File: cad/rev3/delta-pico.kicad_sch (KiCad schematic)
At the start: 70 parts, among them J1 Conn_01x02, J2 Conn_01x14, J3 Conn_01x08, J4 Conn_01x04, J5 Conn_01x03, SW1 SW_SPDT, SW10 SW_Push, SW11 SW_Push, SW12 SW_Push, SW13 SW_Push, SW14 SW_Push, SW15 SW_Push, SW16 SW_Push, SW17 SW_Push, SW18 SW_Push, SW19 SW_Push, SW2 SW_Push, SW20 SW_Push, SW21 SW_Push, SW22 SW_Push, SW23 SW_Push, SW24 SW_Push, SW25 SW_Push, SW26 SW_Push, SW27 SW_Push, SW28 SW_Push, SW29 SW_Push, SW3 SW_Push, SW30 SW_Push, SW31 SW_Push, SW4 SW_Push, SW5 SW_Push, SW6 SW_Push, SW7 SW_Push, SW8 SW_Push, SW9 SW_Push, U1 PCF8574A, U2 PCF8574A, U3 Pico, U4 24LC16

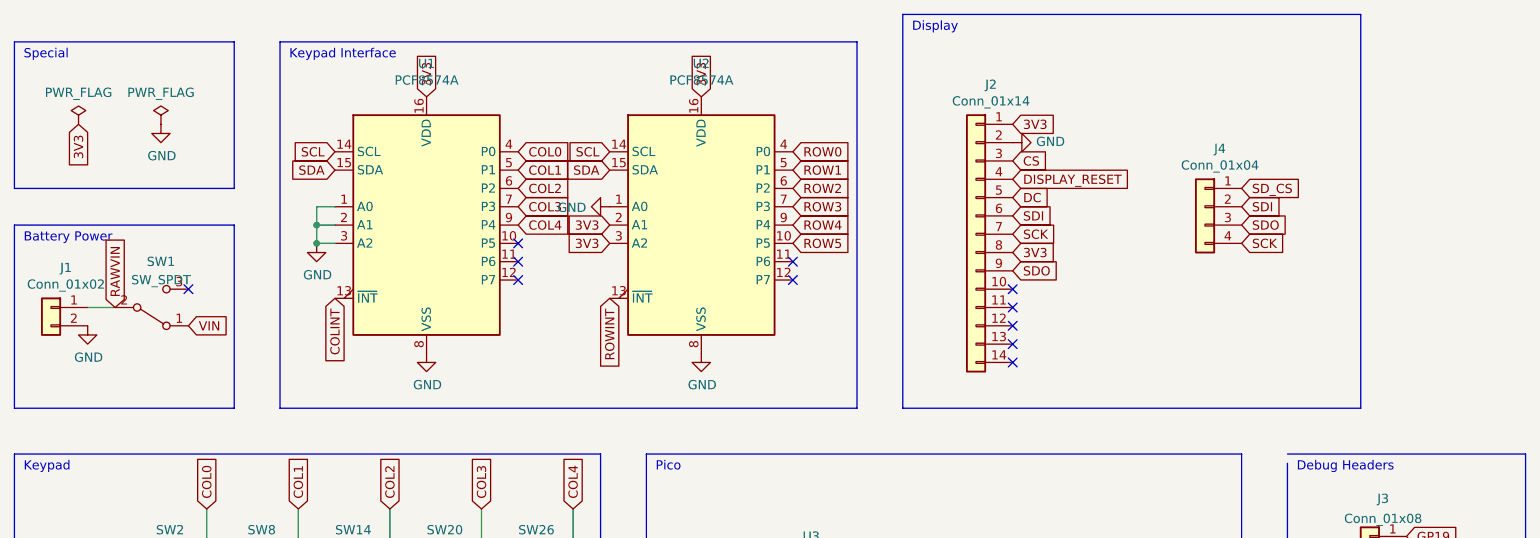
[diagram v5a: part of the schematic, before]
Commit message: Add Schottky diode on VSYS
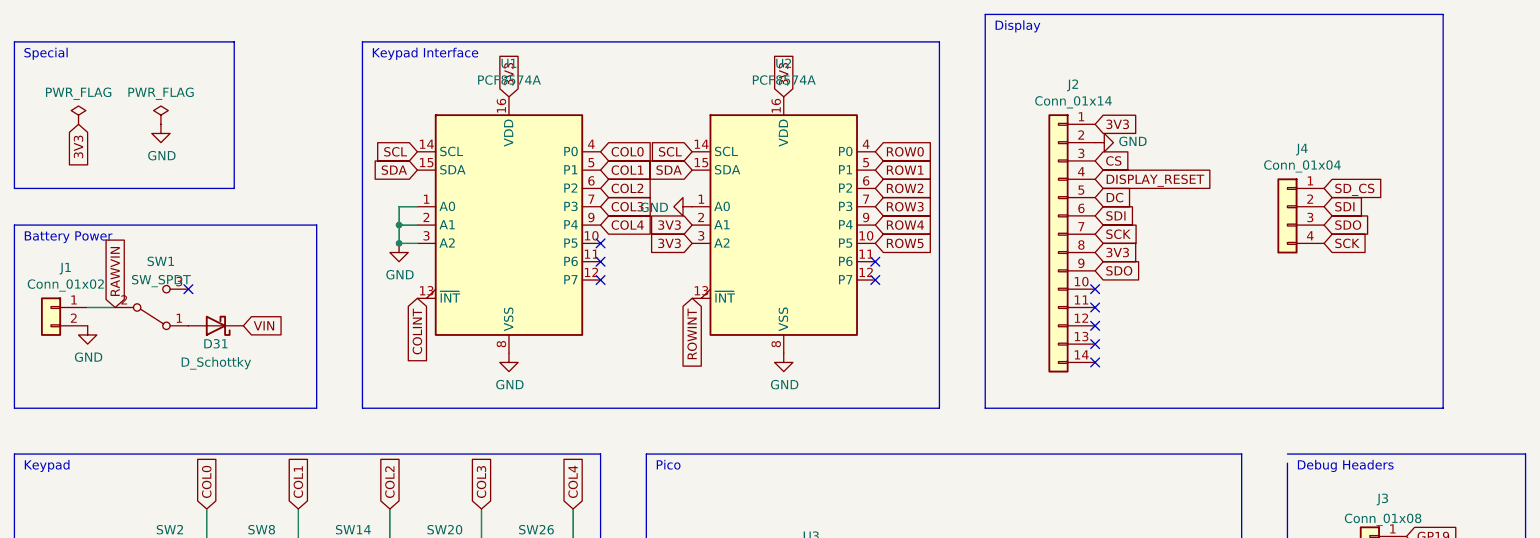
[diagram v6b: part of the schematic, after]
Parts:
- added D31: D_Schottky, Diode_SMD:D_SOD-123, symbol Device:D_Schottky
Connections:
- net VIN: now also D31.1 (K); no longer SW1.1 (A)
- new net: D31.2 (A), SW1.1 (A)
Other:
- moved on the sheet: J2, J4, U1, U2

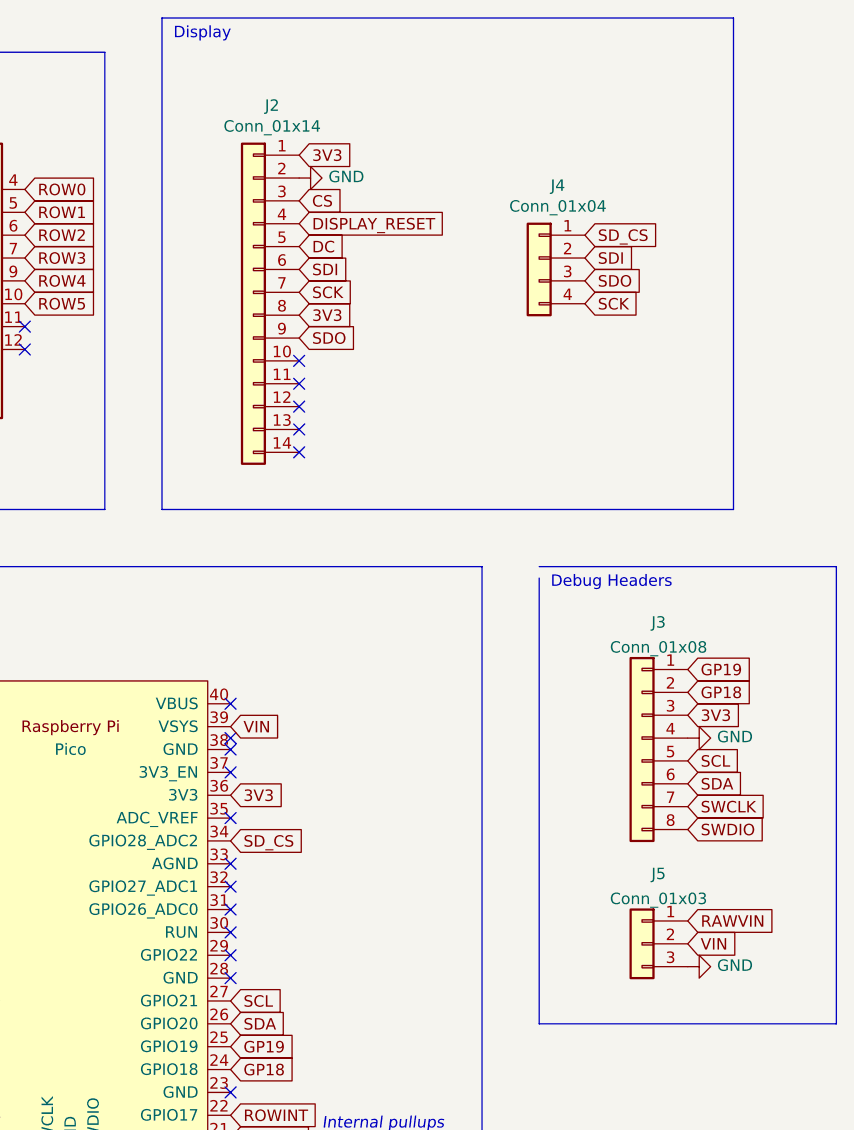
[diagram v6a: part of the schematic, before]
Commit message: Add MOSFET for display power control
And if that doesn't work, there's a jumper to bypass it
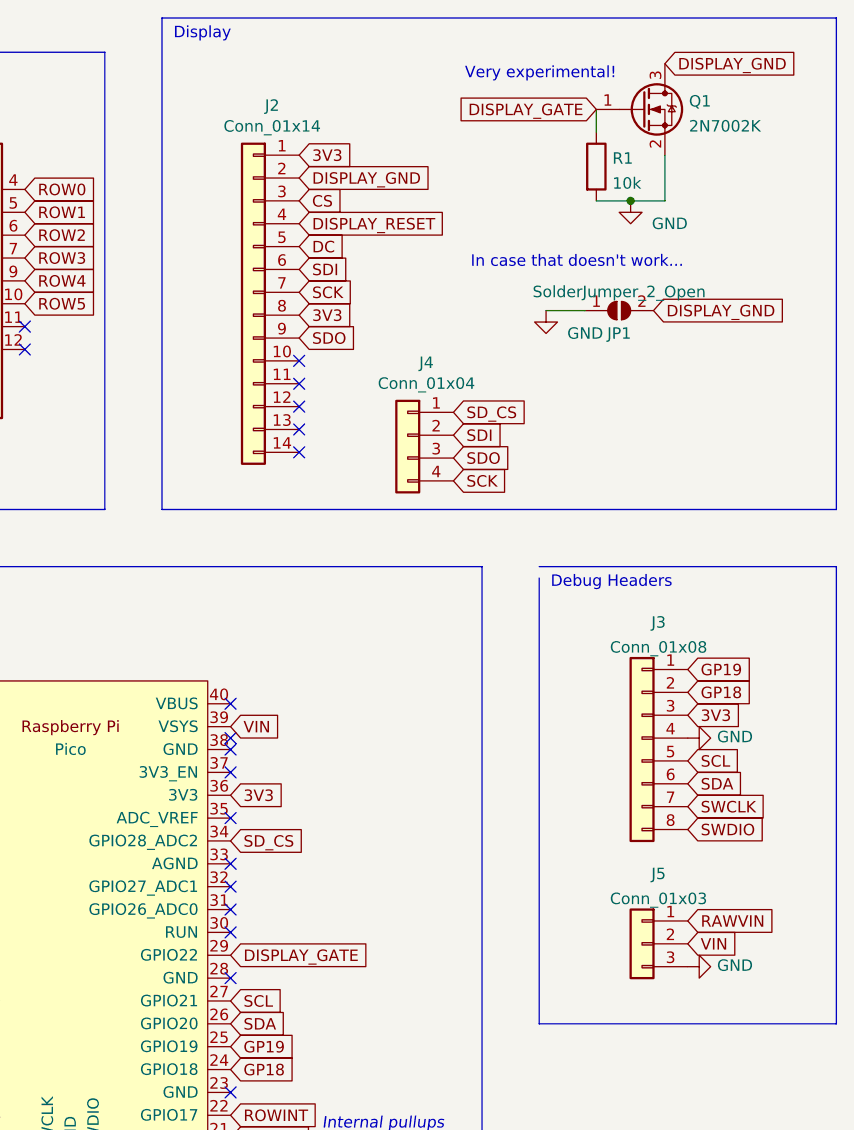
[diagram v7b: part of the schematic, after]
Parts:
- added JP1: SolderJumper_2_Open, Jumper:SolderJumper-2_P1.3mm_Open_RoundedPad1.0x1.5mm, symbol Jumper:SolderJumper_2_Open
- added Q1: 2N7002K, Package_TO_SOT_SMD:SOT-23, symbol Transistor_FET:2N7002K
- added R1: 10k, Resistor_SMD:R_0603_1608Metric_Pad0.98x0.95mm_HandSolder, symbol Device:R
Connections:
- net GND: now also JP1.1 (A), Q1.2 (S), R1.2; no longer J2.2 (Pin_2)
- net DISPLAY_GATE: now reaches U3.29 (GPIO22)
- net DISPLAY_GATE: now also Q1.1 (G), R1.1
- new net DISPLAY_GND: J2.2 (Pin_2), JP1.2 (B), Q1.3 (D)
- no-connect marks 37 -> 36
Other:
- note added: "In case that doesn't work..."
- note added: "Very experimental!"
- moved on the sheet: J4

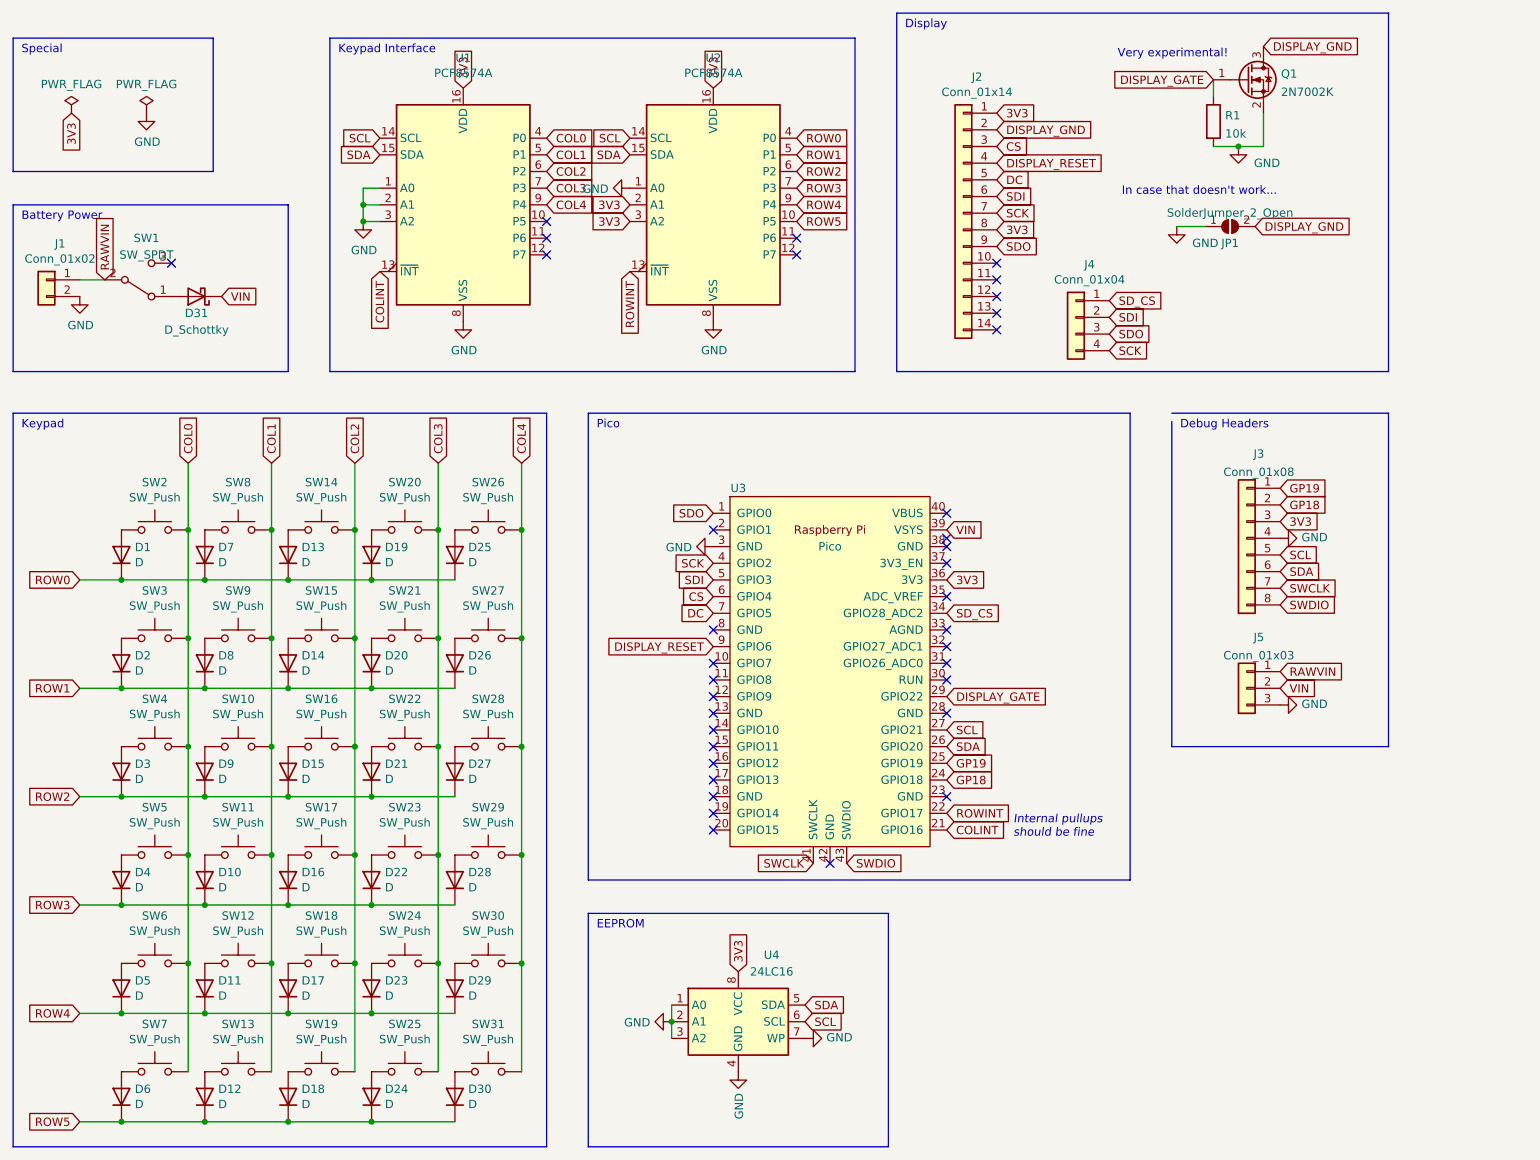
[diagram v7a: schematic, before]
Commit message: Make power switch soft
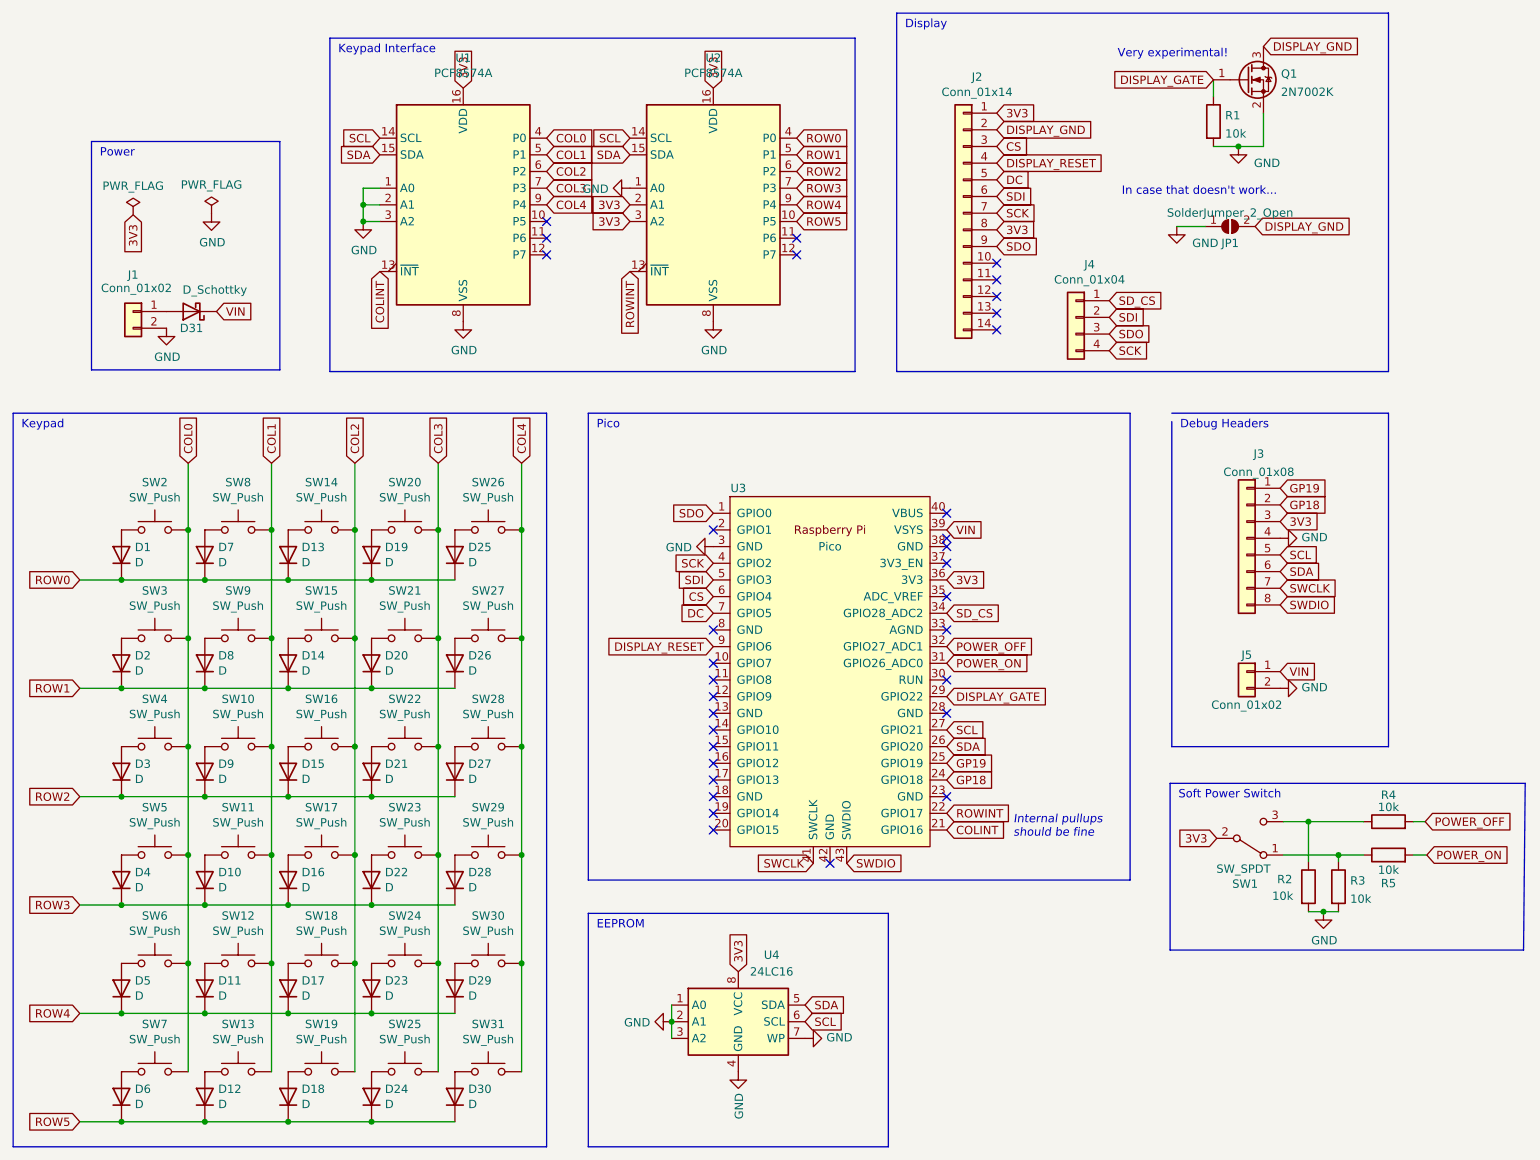
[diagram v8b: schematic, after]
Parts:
- added R2, R3, R4, R5: 10k, Resistor_SMD:R_0603_1608Metric_Pad0.98x0.95mm_HandSolder, symbol Device:R
- J5: value Conn_01x03 -> Conn_01x02; footprint Connector_PinHeader_2.54mm:PinHeader_1x03_P2.54mm_Vertical -> Connector_PinHeader_2.54mm:PinHeader_1x02_P2.54mm_Vertical; symbol Connector_Generic:Conn_01x03 -> Connector_Generic:Conn_01x02
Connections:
- net 3V3: now also SW1.2 (B)
- net GND: now also J5.2 (Pin_2), R2.2, R3.2; no longer J5.3 (Pin_3)
- net VIN: now also J5.1 (Pin_1); no longer J5.2 (Pin_2)
- net POWER_ON: now reaches U3.31 (GPIO26_ADC0)
- net POWER_ON: now also R5.2
- net POWER_OFF: now reaches U3.32 (GPIO27_ADC1)
- net POWER_OFF: now also R4.2
- net at D31.2 (A): now also J1.1 (Pin_1); no longer SW1.1 (A)
- net at SW1.3 (C): now also R2.1, R4.1
- removed net RAWVIN: J1.1 (Pin_1), J5.1 (Pin_1), SW1.2 (B)
- new net: R3.1, R5.1, SW1.1 (A)
- no-connect marks 36 -> 33
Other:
- note added: "Power"
- note added: "Soft Power Switch"
- note removed: "Battery Power"
- note removed: "Special"
- moved on the sheet: D31, J1, SW1
